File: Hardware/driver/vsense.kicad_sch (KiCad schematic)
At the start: 20 parts, among them J601 Screw_Terminal_01x02, K601 EC2-5TNU, U601 MCP3421A1T-ECH, U602 OPA277

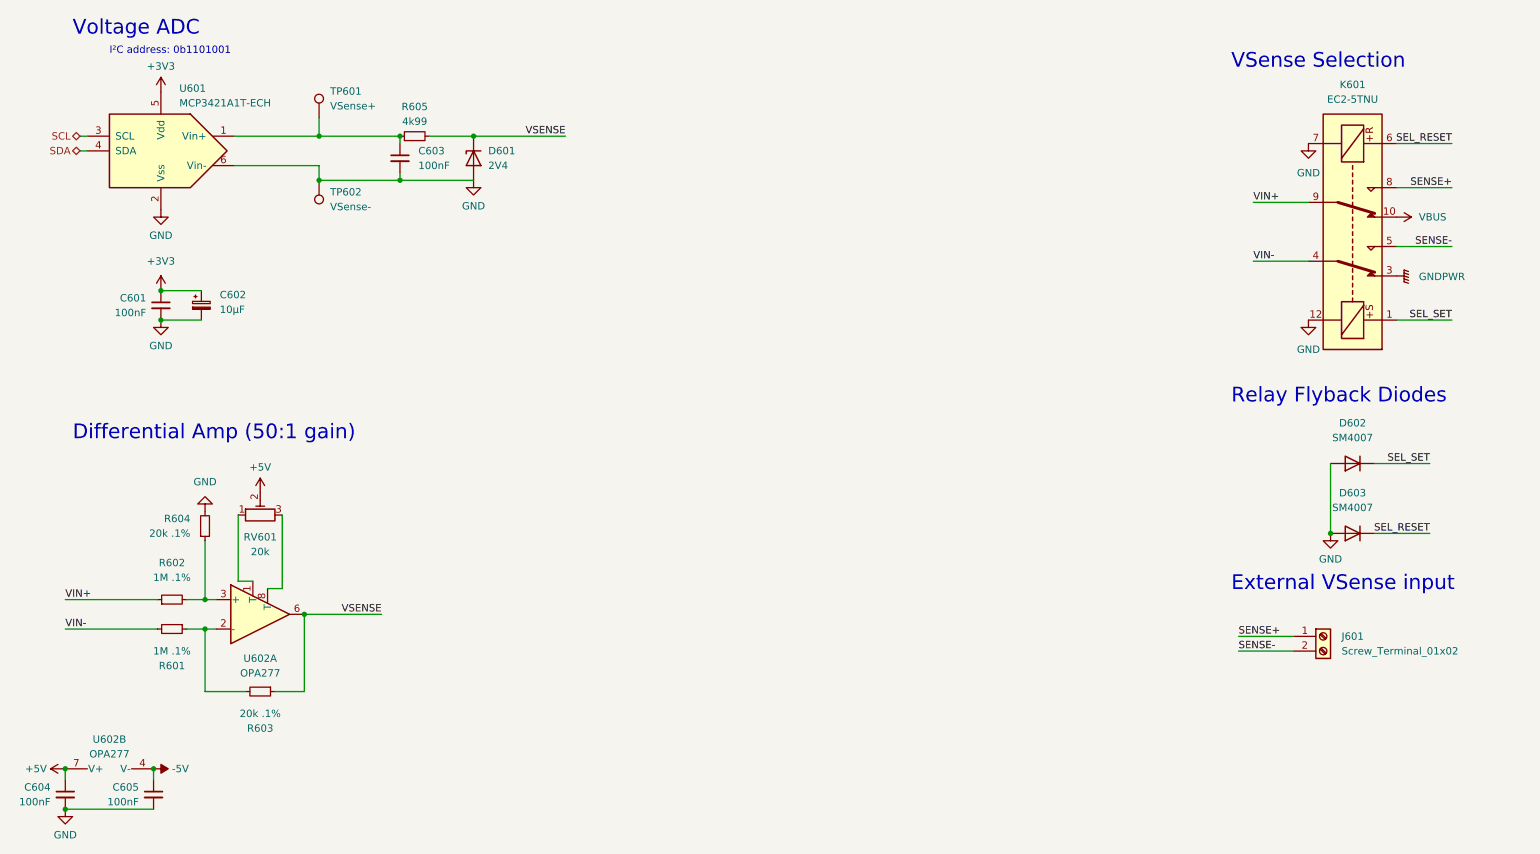
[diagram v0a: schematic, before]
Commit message: Finished remote VSense support
- Laid out the VSense amp and analog-to-digital converter, as well as
  added an I2C IO expander to handle driving the latching relay to
  switch between internal and external sense.

  Also moved the input connector and some of the analog parts around to
  accomodate this all.

- Status indicator (with an extra GPIO on the IO expander) in the form
  of a single LED
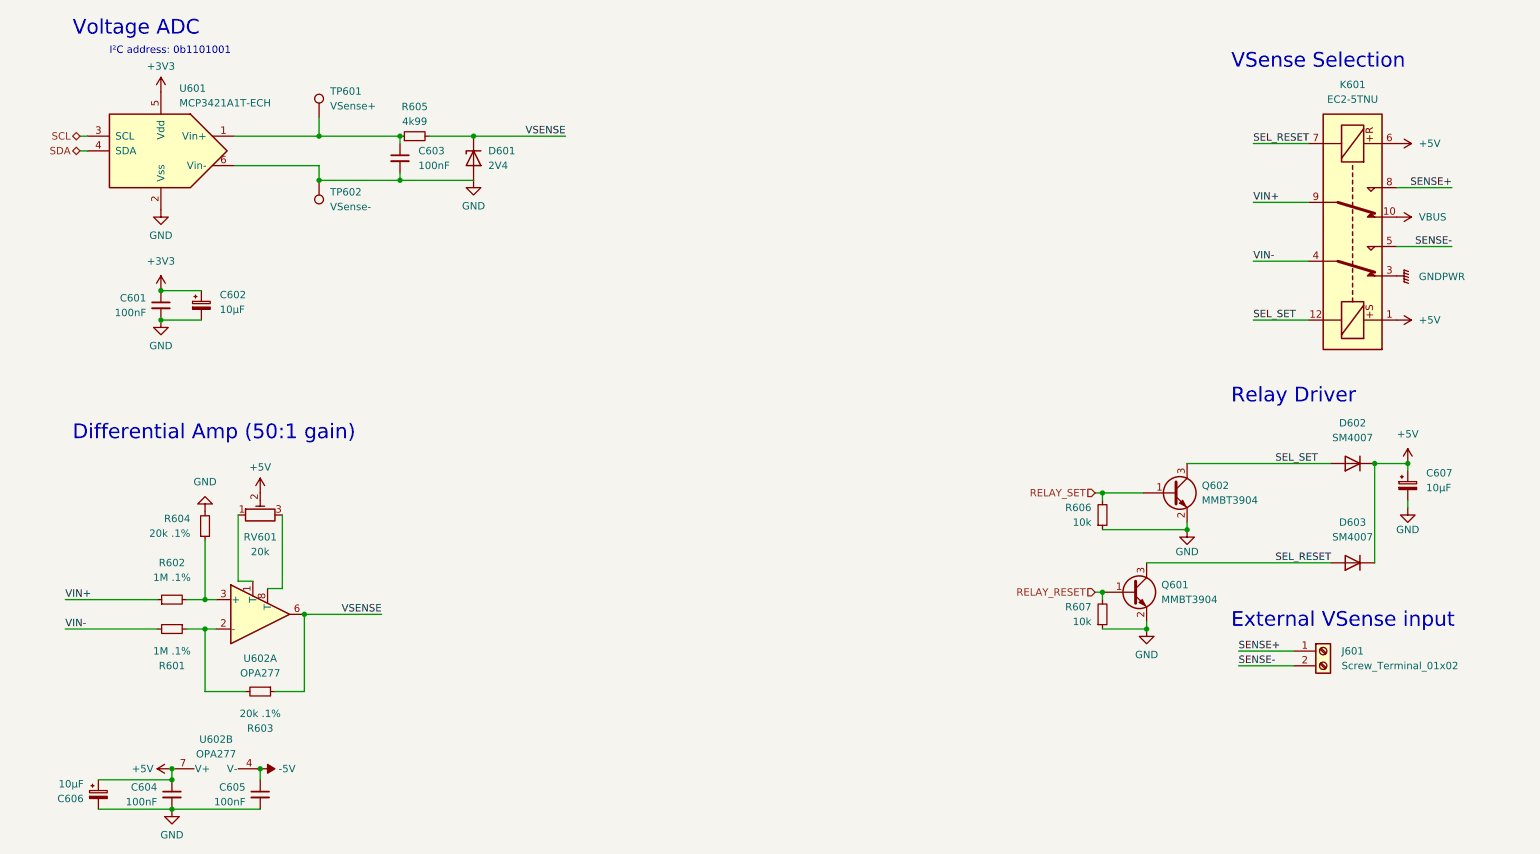
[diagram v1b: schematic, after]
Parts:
- added C606: 10µF, Capacitor_Tantalum_SMD:CP_EIA-3216-18_Kemet-A_Pad1.58x1.35mm_HandSolder, symbol Device:C_Polarized_Small
- added C607: 10µF, Capacitor_THT:C_Radial_D5.0mm_H11.0mm_P2.00mm, symbol Device:C_Polarized_Small
- added Q601, Q602: MMBT3904, Package_TO_SOT_SMD:SOT-23, symbol Transistor_BJT:MMBT3904
- added R606, R607: 10k, Resistor_SMD:R_0805_2012Metric_Pad1.20x1.40mm_HandSolder, symbol Device:R_Small
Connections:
- net +5V: now also D602.1 (K), D603.1 (K), K601.1, K601.6, C606.1, C607.1
- net GND: now also C606.2, C607.2, Q601.2 (E), Q602.2 (E), R606.1, R607.1; no longer D602.2 (A), D603.2 (A), K601.12, K601.7
- net SEL_RESET: now also D603.2 (A), K601.7, Q601.3 (C); no longer D603.1 (K), K601.6
- net SEL_SET: now also D602.2 (A), K601.12, Q602.3 (C); no longer D602.1 (K), K601.1
- new net RELAY_RESET: Q601.1 (B), R607.2
- new net RELAY_SET: Q602.1 (B), R606.2
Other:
- note added: "Relay Driver"
- note removed: "Relay Flyback Diodes"
- moved on the sheet: C604, C605, D603, J601, U602B

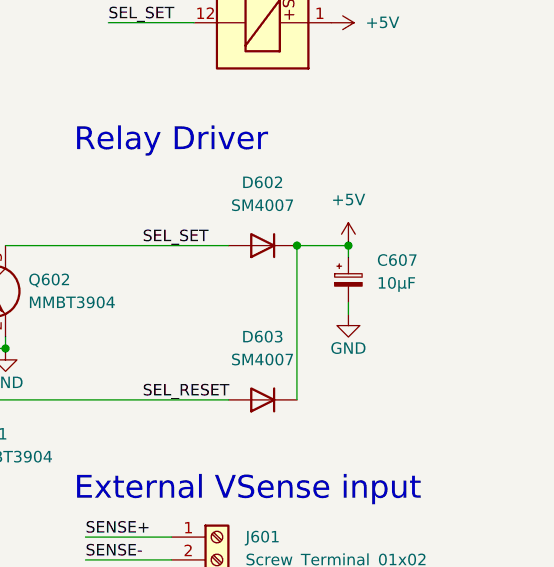
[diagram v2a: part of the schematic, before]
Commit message: More work on rev2 driver board
- Tweaked the board layout for the load driver some more, primarily
  relating to power and friends

- Fixed footprint of fan connector on driver board (to properly have the
  mechanical mounting hole)

- Manufacturability/solderability tweaks for a few other footprints
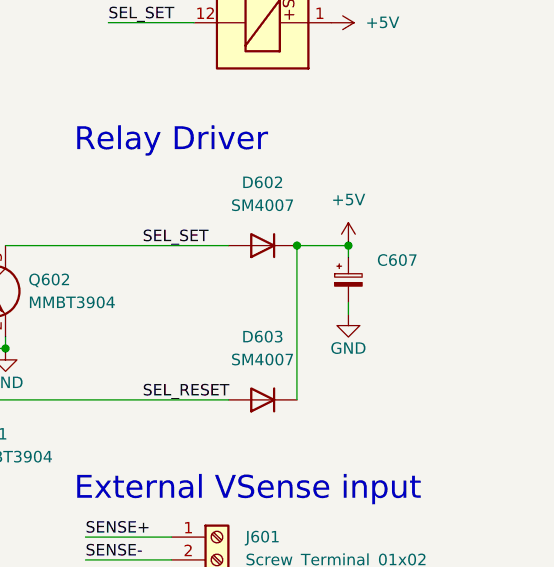
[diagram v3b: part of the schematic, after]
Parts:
- C607: value 10µF -> (none); footprint Capacitor_THT:C_Radial_D5.0mm_H11.0mm_P2.00mm -> (none)
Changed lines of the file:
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@@
       (effects (font (size 1.27 1.27)) (justify left))
     )
-    (property "Value" "10µF" (id 1) (at 259.08 103.2509 0)
+    (property "Value" "" (id 1) (at 259.08 103.2509 0)
       (effects (font (size 1.27 1.27)) (justify left))
     )
-    (property "Footprint" "Capacitor_THT:C_Radial_D5.0mm_H11.0mm_P2.00mm" (id 2) (at 255.905 102.87 0)
+    (property "Footprint" "" (id 2) (at 255.905 102.87 0)
       (effects (font (size 1.27 1.27)) hide)
     )

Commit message: Fixed I2C bus reversal on driver
- Fixed an issue where SCL and SDA for the I2C bus were swapped beyond
  the interface sheet, meaning only the EEPROM is accessible over the
  bus. (This can probably be bodged relatively simply on a rev1 board on
  the bottom where the I2C bus runs)

- Manufacturability tweaks for TDK choke
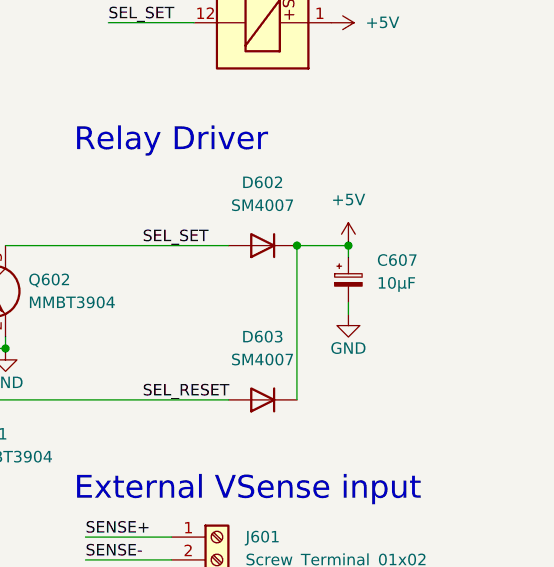
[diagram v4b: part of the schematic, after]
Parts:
- C607: value (none) -> 10µF; footprint (none) -> Capacitor_THT:CP_Radial_D5.0mm_P2.00mm
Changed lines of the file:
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@@
       (effects (font (size 1.27 1.27)) (justify left))
     )
-    (property "Value" "" (id 1) (at 259.08 103.2509 0)
+    (property "Value" "10µF" (id 1) (at 259.08 103.2509 0)
       (effects (font (size 1.27 1.27)) (justify left))
     )
-    (property "Footprint" "" (id 2) (at 255.905 102.87 0)
+    (property "Footprint" "Capacitor_THT:CP_Radial_D5.0mm_P2.00mm" (id 2) (at 255.905 102.87 0)
       (effects (font (size 1.27 1.27)) hide)
     )

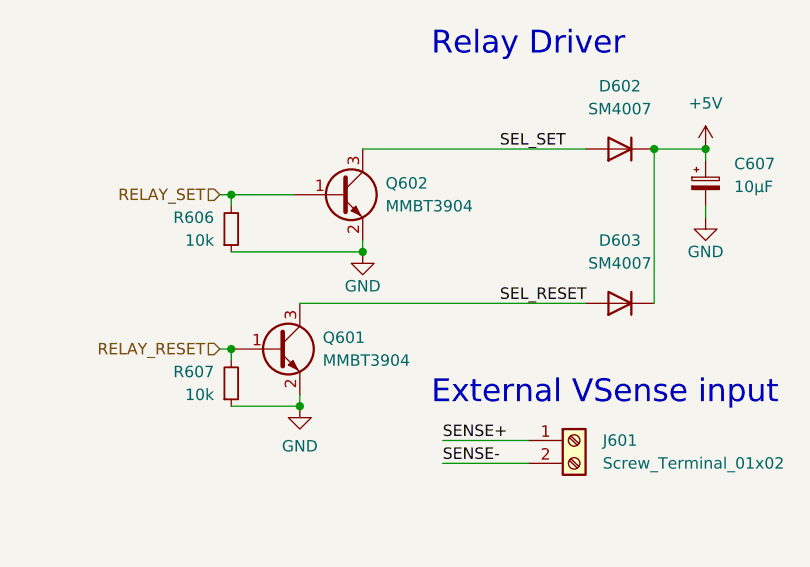
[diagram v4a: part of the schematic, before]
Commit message: Final bits of tweaks for rev2 analog board
- Fixed footprint of MMBT3904 transistors on driver and controller
  boards (it is SOT-323, not SC-70)

- A few more minor modifications to the layout of the analog driver
  board for rev2
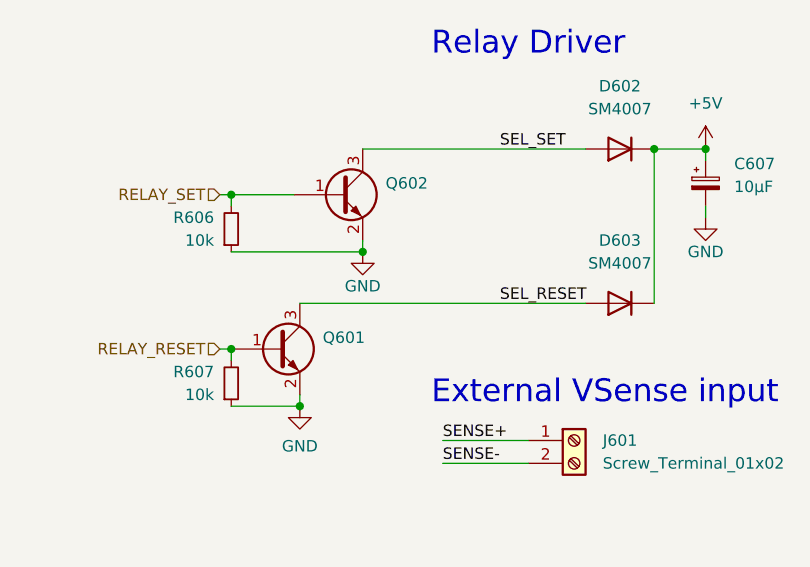
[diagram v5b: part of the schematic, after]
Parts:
- Q601, Q602: value MMBT3904 -> (none); footprint Package_TO_SOT_SMD:SOT-23 -> (none)
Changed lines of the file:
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@@
       (effects (font (size 1.27 1.27)) (justify left))
     )
-    (property "Value" "MMBT3904" (id 1) (at 220.345 105.4099 0)
+    (property "Value" "" (id 1) (at 220.345 105.4099 0)
       (effects (font (size 1.27 1.27)) (justify left))
     )
-    (property "Footprint" "Package_TO_SOT_SMD:SOT-23" (id 2) (at 220.345 106.045 0)
+    (property "Footprint" "" (id 2) (at 220.345 106.045 0)
       (effects (font (size 1.27 1.27) italic) (justify left) hide)
     )
@@
       (effects (font (size 1.27 1.27)) (justify left))
     )
-    (property "Value" "MMBT3904" (id 1) (at 213.36 122.5549 0)
+    (property "Value" "" (id 1) (at 213.36 122.5549 0)
       (effects (font (size 1.27 1.27)) (justify left))
     )
-    (property "Footprint" "Package_TO_SOT_SMD:SOT-23" (id 2) (at 213.36 123.19 0)
+    (property "Footprint" "" (id 2) (at 213.36 123.19 0)
       (effects (font (size 1.27 1.27) italic) (justify left) hide)
     )

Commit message: Fixed a few more footprints
- Made heatsink and connector mechanical/mounting pads NPTH instead of
  normal pads, so they're not tempted to be connected to regular signals
  on the board and get more keepout space
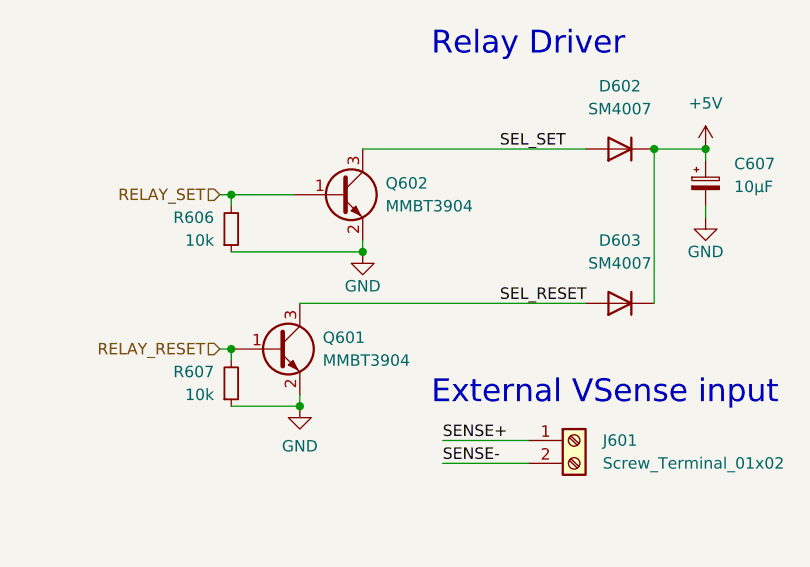
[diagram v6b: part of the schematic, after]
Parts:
- Q601, Q602: value (none) -> MMBT3904; footprint (none) -> Package_TO_SOT_SMD:SOT-323_SC-70_Handsoldering
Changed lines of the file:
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@@
       (effects (font (size 1.27 1.27)) (justify left))
     )
-    (property "Value" "" (id 1) (at 220.345 105.4099 0)
+    (property "Value" "MMBT3904" (id 1) (at 220.345 105.4099 0)
       (effects (font (size 1.27 1.27)) (justify left))
     )
-    (property "Footprint" "" (id 2) (at 220.345 106.045 0)
+    (property "Footprint" "Package_TO_SOT_SMD:SOT-323_SC-70_Handsoldering" (id 2) (at 220.345 106.045 0)
       (effects (font (size 1.27 1.27) italic) (justify left) hide)
     )
@@
       (effects (font (size 1.27 1.27)) (justify left))
     )
-    (property "Value" "" (id 1) (at 213.36 122.5549 0)
+    (property "Value" "MMBT3904" (id 1) (at 213.36 122.5549 0)
       (effects (font (size 1.27 1.27)) (justify left))
     )
-    (property "Footprint" "" (id 2) (at 213.36 123.19 0)
+    (property "Footprint" "Package_TO_SOT_SMD:SOT-323_SC-70_Handsoldering" (id 2) (at 213.36 123.19 0)
       (effects (font (size 1.27 1.27) italic) (justify left) hide)
     )

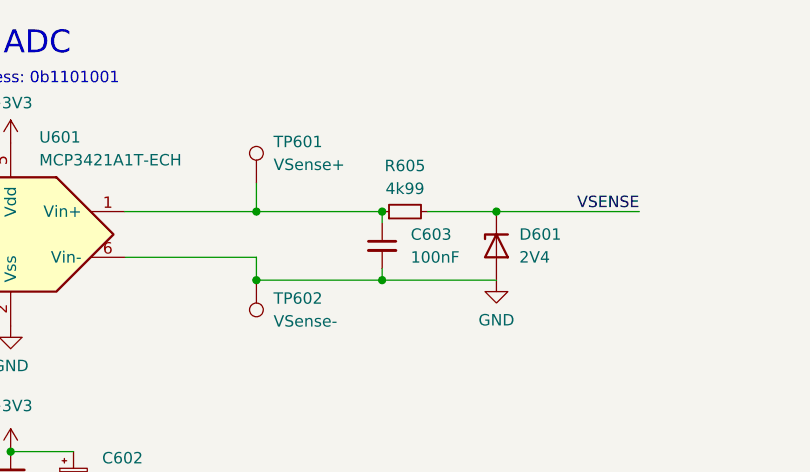
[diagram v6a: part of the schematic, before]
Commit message: Add some missing part numbers to analog board
- Some components on analog load were missing part numbers, so this adds
  them. It also fixes a few components with the same value, where some
  had a part number and others didn't.
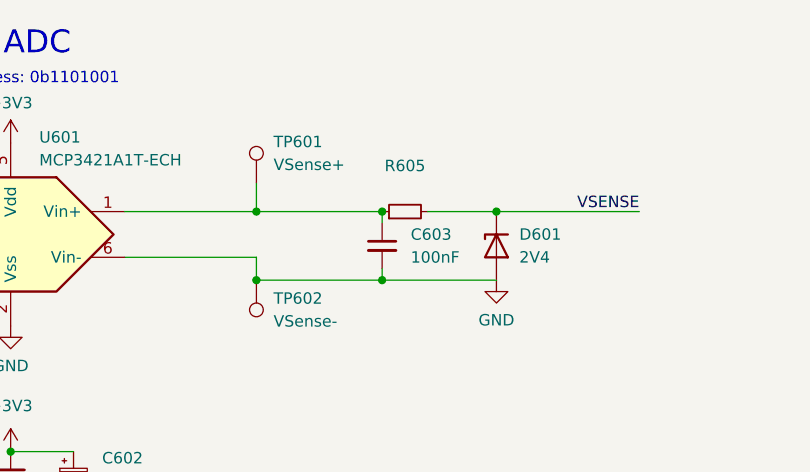
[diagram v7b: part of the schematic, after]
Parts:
- R605: value 4k99 -> (none); footprint Resistor_SMD:R_0805_2012Metric_Pad1.20x1.40mm_HandSolder -> (none); MPN (none) -> CR0805-FX-4991ELF
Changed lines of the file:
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@@
     (in_bom yes) (on_board yes)
     (property "Reference" "R605" (id 0) (at 84.455 37.465 90))
-    (property "Value" "4k99" (id 1) (at 84.455 40.005 90))
-    (property "Footprint" "Resistor_SMD:R_0805_2012Metric_Pad1.20x1.40mm_HandSolder" (id 2) (at 84.455 42.545 0)
+    (property "Value" "" (id 1) (at 84.455 40.005 90))
+    (property "Footprint" "" (id 2) (at 84.455 42.545 0)
       (effects (font (size 1.27 1.27)) hide)
     )
@@
       (effects (font (size 1.27 1.27)) hide)
     )
+    (property "MPN" "CR0805-FX-4991ELF" (id 4) (at 84.455 42.545 90)
+      (effects (font (size 1.27 1.27)) hide)
+    )
